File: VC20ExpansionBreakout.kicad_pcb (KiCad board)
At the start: 2 copper layers, 99.1 x 87.9 mm, 11 parts, among them J1 Other, J2 Power, J3 GND, J4 Breakout, J5 NC, SW1 Reset, U1 VC20-Exp-Port, U2 27C512/27C020

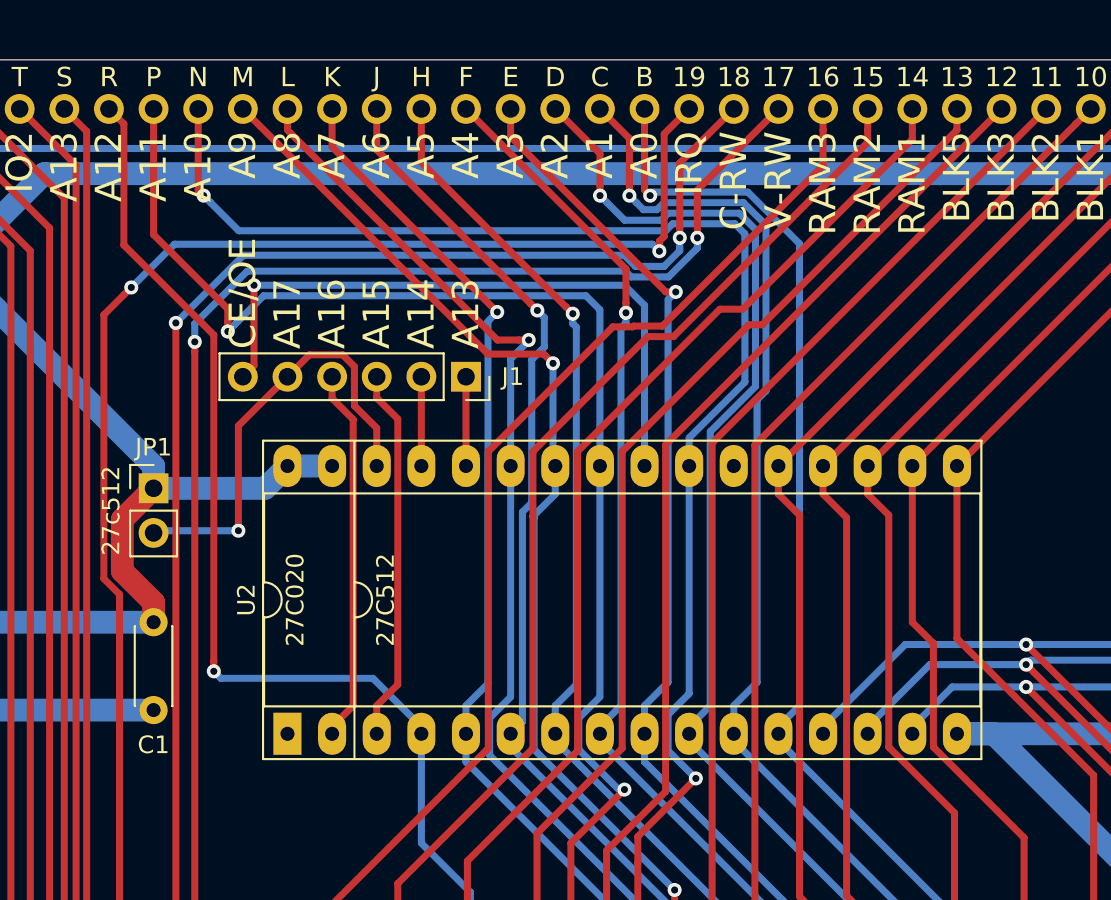
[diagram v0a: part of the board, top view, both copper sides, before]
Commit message: Added missing connections.
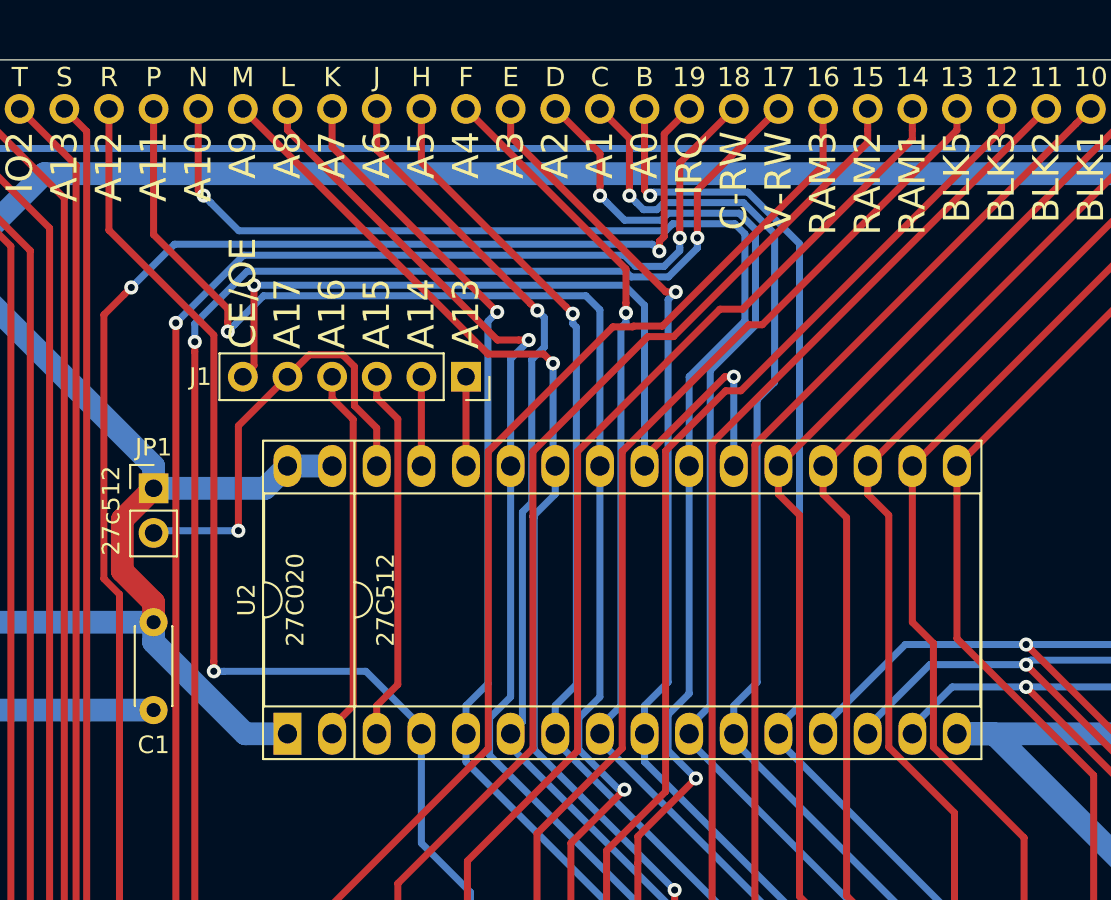
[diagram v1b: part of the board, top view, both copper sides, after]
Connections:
- net RST renamed /RST
- U2 pad 1: Net-(U2-Pad1) -> +5V
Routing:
- net /CE: track 37.3 -> 49.9 mm, vias 1 -> 2
- net +5V: track 102.9 -> 113.8 mm
- net /BLK3: track 88.8 -> 89.3 mm

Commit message: Fixing silk-screen.
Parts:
- moved G*** 3.30 mm to (179.1, 104.6)
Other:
- outline, holes or cut-outs redrawn
- board text added: "20"
- board text added: "github.com/hackup/VC20ExpansionBreakout Rev.1"
- board text removed: "Rev.1 github.com/hackup/VC20ExpansionBreakout"
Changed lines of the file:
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@@
   (general
     (thickness 1.6)
-    (drawings 103)
+    (drawings 105)
     (tracks 558)
     (zones 0)
@@
   )
   (module Logo:bigby2 (layer F.Cu)
-    (at 180.7464 107.4928)
+    (at 179.07 104.648)
     (fp_text reference G*** (at 0 0) (layer F.SilkS) hide
       (effects (font (size 1.524 1.524) (thickness 0.3)))
@@
     )
   )
+  (gr_line (start 184.15 101.727) (end 182.52 101.727) (layer Edge.Cuts) (width 0.05))
+  (gr_line (start 185.42 100.457) (end 184.15 101.727) (layer Edge.Cuts) (width 0.05))
+  (gr_line (start 185.42 65.786) (end 185.42 100.457) (layer Edge.Cuts) (width 0.05))
+  (gr_line (start 182.52 141.4) (end 182.52 101.727) (layer Edge.Cuts) (width 0.05))
   (gr_text Y (at 93.98 85.344) (layer F.SilkS)
     (effects (font (size 1.1 1.1) (thickness 0.2)))
   )
-  (gr_text 19 (at 96.52 85.344) (layer F.SilkS)
+  (gr_text 20 (at 96.52 85.344) (layer F.SilkS)
     (effects (font (size 1.1 1.1) (thickness 0.2)))
   )
@@
     (effects (font (size 1.5 1.5) (thickness 0.3)) (justify left))
   )
-  (gr_text "Rev.1\ngithub.com/hackup/VC20ExpansionBreakout" (at 182.626 116.2304 90) (layer F.SilkS)
-    (effects (font (size 1.5 1.5) (thickness 0.3)) (justify left))
+  (gr_text "github.com/hackup/VC20ExpansionBreakout\nRev.1" (at 181.229 109.22) (layer F.SilkS)
+    (effects (font (size 1.5 1.5) (thickness 0.3)) (justify right))
   )
   (gr_text D0 (at 180.34 68.58 90) (layer F.SilkS)
@@
     (effects (font (size 1 1) (thickness 0.2)))
   )
-  (gr_line (start 185.42 141.4) (end 185.42 139.7) (layer Edge.Cuts) (width 0.05))
-  (gr_line (start 179.98 141.4) (end 185.42 141.4) (layer Edge.Cuts) (width 0.05))
-  (gr_line (start 185.42 65.786) (end 185.42 139.7) (layer Edge.Cuts) (width 0.05))
+  (gr_line (start 179.98 141.4) (end 182.52 141.4) (layer Edge.Cuts) (width 0.05))
   (gr_line (start 87.63 64.516) (end 184.15 64.516) (layer Edge.Cuts) (width 0.05))
   (gr_line (start 86.36 141.4) (end 86.36 65.786) (layer Edge.Cuts) (width 0.05))

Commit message: Fine tuning.
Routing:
- net GND: track 318.3 -> 323.2 mm, vias 10 -> 12
- net +5V: track 113.8 -> 116.3 mm, vias 1 -> 2
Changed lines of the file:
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@@
     (thickness 1.6)
     (drawings 105)
-    (tracks 558)
+    (tracks 565)
     (zones 0)
     (modules 11)
@@
   (segment (start 106.68 96.52) (end 106.68 97.65137) (width 1.3) (layer B.Cu) (net 1))
   (segment (start 106.68 97.65137) (end 111.89863 102.87) (width 1.3) (layer B.Cu) (net 1))
+  (via (at 93.345 99.695) (size 0.8) (drill 0.4) (layers F.Cu B.Cu) (net 1))
+  (segment (start 93.472 97.282) (end 93.472 99.568) (width 1.3) (layer B.Cu) (net 1))
+  (segment (start 93.472 99.568) (end 93.345 99.695) (width 1.3) (layer B.Cu) (net 1))
   (segment (start 176.02 141.9) (end 176.02 146.8) (width 1.3) (layer B.Cu) (net 2))
   (segment (start 176.02 124.39) (end 176.02 131.574) (width 1.3) (layer B.Cu) (net 2))
@@
   (segment (start 168.852315 102.87) (end 152.4 102.87) (width 1.3) (layer B.Cu) (net 2))
   (segment (start 169.418 102.87) (end 168.852315 102.87) (width 1.3) (layer B.Cu) (net 2))
-  (segment (start 106.68 101.52) (end 92.223991 101.52) (width 1.3) (layer B.Cu) (net 2))
-  (segment (start 92.223991 101.52) (end 92.09499 101.649001) (width 1.3) (layer B.Cu) (net 2))
   (segment (start 92.777919 74.93) (end 93.98 74.93) (width 1.3) (layer F.Cu) (net 2))
   (segment (start 91.463989 76.24393) (end 92.777919 74.93) (width 1.3) (layer F.Cu) (net 2))
-  (via (at 92.09499 101.649001) (size 0.8) (drill 0.4) (layers F.Cu B.Cu) (net 2))
   (via (at 91.463989 131.087989) (size 0.8) (drill 0.4) (layers F.Cu B.Cu) (net 2))
   (segment (start 91.463989 131.087989) (end 91.463989 76.24393) (width 1.3) (layer F.Cu) (net 2))
@@
   (segment (start 92.86 141.0184) (end 92.86 146.8) (width 1.3) (layer B.Cu) (net 2))
   (segment (start 91.463989 139.622389) (end 92.86 141.0184) (width 1.3) (layer B.Cu) (net 2))
+  (via (at 91.463989 101.576011) (size 0.8) (drill 0.4) (layers F.Cu B.Cu) (net 2))
+  (segment (start 106.68 101.52) (end 91.52 101.52) (width 1.3) (layer B.Cu) (net 2))
+  (segment (start 91.52 101.52) (end 91.463989 101.576011) (width 1.3) (layer B.Cu) (net 2))
+  (via (at 91.463989 104.116011) (size 0.8) (drill 0.4) (layers F.Cu B.Cu) (net 2))
+  (segment (start 91.463989 101.576011) (end 91.463989 104.116011) (width 1.3) (layer B.Cu) (net 2))
+  (via (at 167.64 102.87) (size 0.8) (drill 0.4) (layers F.Cu B.Cu) (net 2))
+  (segment (start 169.418 102.87) (end 167.64 102.87) (width 1.3) (layer F.Cu) (net 2))
   (segment (start 124.46 82.55) (end 124.46 87.63) (width 0.4) (layer F.Cu) (net 3))
   (segment (start 121.92 83.752081) (end 121.92 87.63) (width 0.4) (layer F.Cu) (net 4))
